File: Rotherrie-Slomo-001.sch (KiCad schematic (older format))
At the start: 17 parts, among them U1 TL074

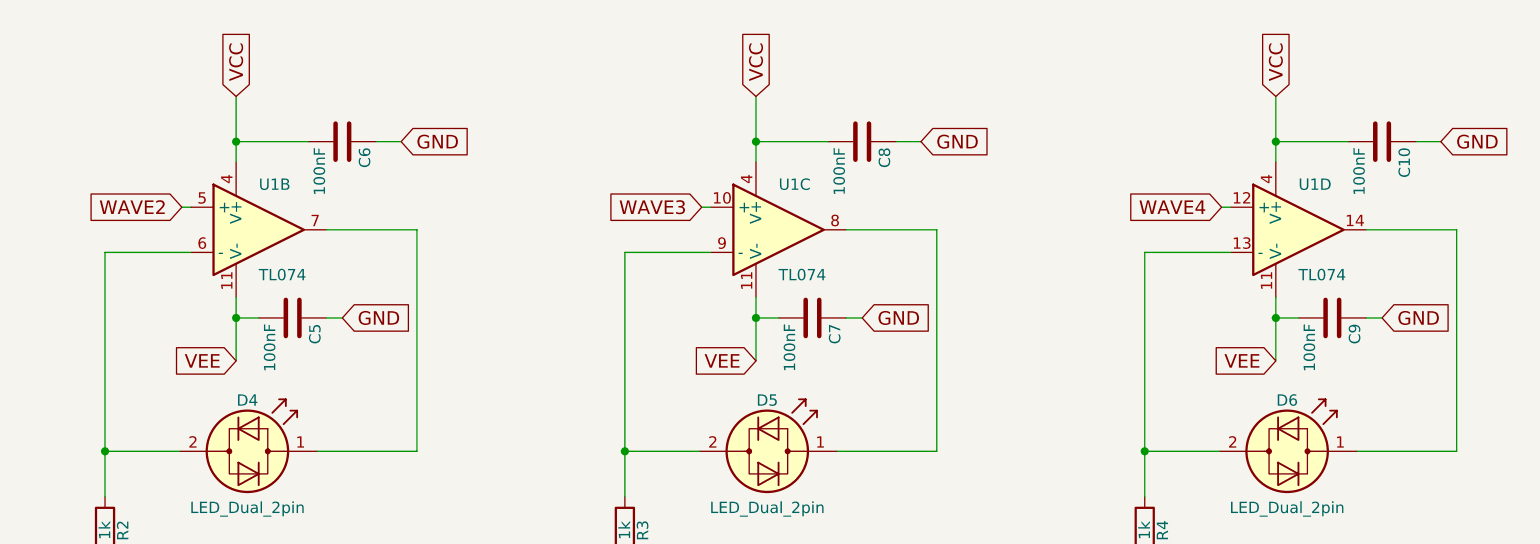
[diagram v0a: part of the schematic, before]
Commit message: Part associations made. 16pin connector reduced to 10 pin
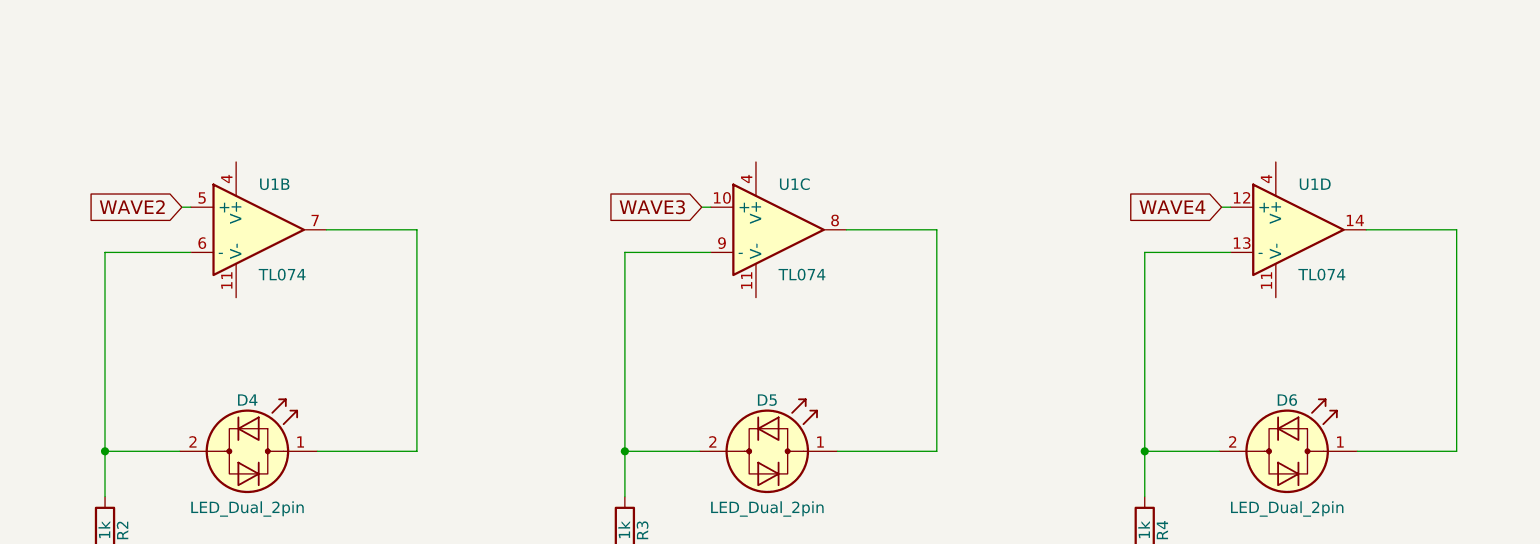
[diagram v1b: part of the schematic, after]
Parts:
- removed C10, C5, C6, C7, C8, C9: 100nF, symbol C
- C3, C4: footprint (none) -> Capacitors_THT:C_Disc_D4.3mm_W1.9mm_P5.00mm
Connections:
- net VCC: no longer U1.4 (V+), U1.4 (V+), U1.4 (V+)
- net VEE: no longer U1.11 (V-), U1.11 (V-), U1.11 (V-)
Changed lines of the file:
@@
 F 0 "C3" H 2625 3140 50  0000 L CNN
 F 1 "100nF" H 2625 2940 50  0000 L CNN
-F 2 "" H 2638 2890 50  0001 C CNN
+F 2 "Capacitors_THT:C_Disc_D4.3mm_W1.9mm_P5.00mm" H 2638 2890 50  0001 C CNN
 F 3 "" H 2600 3040 50  0001 C CNN
 	1    2600 3040
@@
 F 0 "C4" H 2845 2360 50  0000 L CNN
 F 1 "100nF" H 2845 2160 50  0000 L CNN
-F 2 "" H 2858 2110 50  0001 C CNN
+F 2 "Capacitors_THT:C_Disc_D4.3mm_W1.9mm_P5.00mm" H 2858 2110 50  0001 C CNN
 F 3 "" H 2820 2260 50  0001 C CNN
 	1    2820 2260
@@
 	1    0    0    -1
 $EndComp
-Text GLabel 4650 2060 1    60   Input ~ 0
-VCC
-Text GLabel 4650 3230 0    60   Input ~ 0
-VEE
 $Comp
 L LED_Dual_2pin D4
@@
 	1    0    0    -1
 $EndComp
-$Comp
-L C C5
-U 1 1 59B166A0
-P 4900 3040
-F 0 "C5" H 4925 3140 50  0000 L CNN
-F 1 "100nF" H 4925 2940 50  0000 L CNN
-F 2 "" H 4938 2890 50  0001 C CNN
-F 3 "" H 4900 3040 50  0001 C CNN
-	1    4900 3040
-	0    1    1    0
-$EndComp
-Text GLabel 5120 3040 2    60   Input ~ 0
-GND
-$Comp
-L C C6
-U 1 1 59B166B5
-P 5120 2260
-F 0 "C6" H 5145 2360 50  0000 L CNN
-F 1 "100nF" H 5145 2160 50  0000 L CNN
-F 2 "" H 5158 2110 50  0001 C CNN
-F 3 "" H 5120 2260 50  0001 C CNN
-	1    5120 2260
-	0    1    1    0
-$EndComp
-Text GLabel 5380 2260 2    60   Input ~ 0
-GND
 Text GLabel 6370 4300 3    60   Input ~ 0
 GND
@@
 	1    0    0    -1
 $EndComp
-Text GLabel 6950 2060 1    60   Input ~ 0
-VCC
-Text GLabel 6950 3230 0    60   Input ~ 0
-VEE
 $Comp
 L LED_Dual_2pin D5
@@
 	1    0    0    -1
 $EndComp
-$Comp
-L C C7
-U 1 1 59B1681D
-P 7200 3040
-F 0 "C7" H 7225 3140 50  0000 L CNN
-F 1 "100nF" H 7225 2940 50  0000 L CNN
-F 2 "" H 7238 2890 50  0001 C CNN
-F 3 "" H 7200 3040 50  0001 C CNN
-	1    7200 3040
-	0    1    1    0
-$EndComp
-Text GLabel 7420 3040 2    60   Input ~ 0
-GND
-$Comp
-L C C8
-U 1 1 59B16832
-P 7420 2260
-F 0 "C8" H 7445 2360 50  0000 L CNN
-F 1 "100nF" H 7445 2160 50  0000 L CNN
-F 2 "" H 7458 2110 50  0001 C CNN
-F 3 "" H 7420 2260 50  0001 C CNN
-	1    7420 2260
-	0    1    1    0
-$EndComp
-Text GLabel 7680 2260 2    60   Input ~ 0
-GND
 Text GLabel 8670 4300 3    60   Input ~ 0
 GND
@@
 	1    0    0    -1
 $EndComp
-Text GLabel 9250 2060 1    60   Input ~ 0
-VCC
-Text GLabel 9250 3230 0    60   Input ~ 0
-VEE
 $Comp
 L LED_Dual_2pin D6
@@
 	1    0    0    -1
 $EndComp
-$Comp
-L C C9
-U 1 1 59B16A0F
-P 9500 3040
-F 0 "C9" H 9525 3140 50  0000 L CNN
-F 1 "100nF" H 9525 2940 50  0000 L CNN
-F 2 "" H 9538 2890 50  0001 C CNN
-F 3 "" H 9500 3040 50  0001 C CNN
-	1    9500 3040
-	0    1    1    0
-$EndComp
-Text GLabel 9720 3040 2    60   Input ~ 0
-GND
-$Comp
-L C C10
-U 1 1 59B16A24
-P 9720 2260
-F 0 "C10" H 9745 2360 50  0000 L CNN
-F 1 "100nF" H 9745 2160 50  0000 L CNN
-F 2 "" H 9758 2110 50  0001 C CNN
-F 3 "" H 9720 2260 50  0001 C CNN
-	1    9720 2260
-	0    1    1    0
-$EndComp
-Text GLabel 9980 2260 2    60   Input ~ 0
-GND
 Wire Wire Line
 	2350 2060 2350 2350
@@
 	2970 2260 3080 2260
 Wire Wire Line
-	4650 2060 4650 2350
-Wire Wire Line
 	5050 2650 5450 2650
 Wire Wire Line
@@
 	4070 4300 4070 4130
 Wire Wire Line
-	4750 3040 4650 3040
-Connection ~ 4650 3040
-Wire Wire Line
 	5450 2650 5450 3630
-Wire Wire Line
-	5120 3040 5050 3040
 Wire Wire Line
 	5450 3630 5010 3630
@@
 Connection ~ 4070 3630
 Wire Wire Line
-	4650 2950 4650 3230
-Wire Wire Line
 	4410 2550 4450 2550
 Wire Wire Line
-	4970 2260 4650 2260
-Connection ~ 4650 2260
-Wire Wire Line
-	5270 2260 5380 2260
-Wire Wire Line
-	6950 2060 6950 2350
-Wire Wire Line
 	7350 2650 7750 2650
 Wire Wire Line
@@
 	6370 4300 6370 4130
 Wire Wire Line
-	7050 3040 6950 3040
-Connection ~ 6950 3040
-Wire Wire Line
 	7750 2650 7750 3630
-Wire Wire Line
-	7420 3040 7350 3040
 Wire Wire Line
 	7750 3630 7310 3630
@@
 Connection ~ 6370 3630
 Wire Wire Line
-	6950 2950 6950 3230
-Wire Wire Line
 	6710 2550 6750 2550
 Wire Wire Line
-	7270 2260 6950 2260
-Connection ~ 6950 2260
-Wire Wire Line
-	7570 2260 7680 2260
-Wire Wire Line
-	9250 2060 9250 2350
-Wire Wire Line
 	9650 2650 10050 2650
 Wire Wire Line
@@
 	8670 4300 8670 4130
 Wire Wire Line
-	9350 3040 9250 3040
-Connection ~ 9250 3040
-Wire Wire Line
 	10050 2650 10050 3630
-Wire Wire Line
-	9720 3040 9650 3040
 Wire Wire Line
 	10050 3630 9610 3630
@@
 Connection ~ 8670 3630
 Wire Wire Line
-	9250 2950 9250 3230
-Wire Wire Line
 	9010 2550 9050 2550
-Wire Wire Line
-	9570 2260 9250 2260
-Connection ~ 9250 2260
-Wire Wire Line
-	9870 2260 9980 2260
 $EndSCHEMATC

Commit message: Added jack connectors to schematic
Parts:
- D3, D4, D5, D6: footprint (none) -> LEDs:LED_D3.0mm
- R1, R2, R3, R4: footprint (none) -> Resistors_THT:R_Axial_DIN0207_L6.3mm_D2.5mm_P7.62mm_Horizontal
- U1: footprint (none) -> Housings_DIP:DIP-14_W7.62mm_Socket
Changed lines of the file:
@@
 F 0 "U1" H 2450 2850 50  0000 L CNN
 F 1 "TL074" H 2450 2450 50  0000 L CNN
-F 2 "" H 2400 2750 50  0001 C CNN
+F 2 "Housings_DIP:DIP-14_W7.62mm_Socket" H 2400 2750 50  0001 C CNN
 F 3 "" H 2500 2850 50  0001 C CNN
 	1    2450 2650
@@
 F 0 "D3" H 2400 3855 50  0000 C CNN
 F 1 "LED_Dual_2pin" H 2400 3380 50  0000 C CNN
-F 2 "" H 2400 3630 50  0001 C CNN
+F 2 "LEDs:LED_D3.0mm" H 2400 3630 50  0001 C CNN
 F 3 "" H 2400 3630 50  0001 C CNN
 	1    2400 3630
@@
 F 0 "R1" V 1850 3980 50  0000 C CNN
 F 1 "1k" V 1770 3980 50  0000 C CNN
-F 2 "" V 1700 3980 50  0001 C CNN
+F 2 "Resistors_THT:R_Axial_DIN0207_L6.3mm_D2.5mm_P7.62mm_Horizontal" V 1700 3980 50  0001 C CNN
 F 3 "" H 1770 3980 50  0001 C CNN
 	1    1770 3980
@@
 F 0 "U1" H 4750 2850 50  0000 L CNN
 F 1 "TL074" H 4750 2450 50  0000 L CNN
-F 2 "" H 4700 2750 50  0001 C CNN
+F 2 "Housings_DIP:DIP-14_W7.62mm_Socket" H 4700 2750 50  0001 C CNN
 F 3 "" H 4800 2850 50  0001 C CNN
 	2    4750 2650
@@
 F 0 "D4" H 4700 3855 50  0000 C CNN
 F 1 "LED_Dual_2pin" H 4700 3380 50  0000 C CNN
-F 2 "" H 4700 3630 50  0001 C CNN
+F 2 "LEDs:LED_D3.0mm" H 4700 3630 50  0001 C CNN
 F 3 "" H 4700 3630 50  0001 C CNN
 	1    4700 3630
@@
 F 0 "R2" V 4150 3980 50  0000 C CNN
 F 1 "1k" V 4070 3980 50  0000 C CNN
-F 2 "" V 4000 3980 50  0001 C CNN
+F 2 "Resistors_THT:R_Axial_DIN0207_L6.3mm_D2.5mm_P7.62mm_Horizontal" V 4000 3980 50  0001 C CNN
 F 3 "" H 4070 3980 50  0001 C CNN
 	1    4070 3980
@@
 F 0 "U1" H 7050 2850 50  0000 L CNN
 F 1 "TL074" H 7050 2450 50  0000 L CNN
-F 2 "" H 7000 2750 50  0001 C CNN
+F 2 "Housings_DIP:DIP-14_W7.62mm_Socket" H 7000 2750 50  0001 C CNN
 F 3 "" H 7100 2850 50  0001 C CNN
 	3    7050 2650
@@
 F 0 "D5" H 7000 3855 50  0000 C CNN
 F 1 "LED_Dual_2pin" H 7000 3380 50  0000 C CNN
-F 2 "" H 7000 3630 50  0001 C CNN
+F 2 "LEDs:LED_D3.0mm" H 7000 3630 50  0001 C CNN
 F 3 "" H 7000 3630 50  0001 C CNN
 	1    7000 3630
@@
 F 0 "R3" V 6450 3980 50  0000 C CNN
 F 1 "1k" V 6370 3980 50  0000 C CNN
-F 2 "" V 6300 3980 50  0001 C CNN
+F 2 "Resistors_THT:R_Axial_DIN0207_L6.3mm_D2.5mm_P7.62mm_Horizontal" V 6300 3980 50  0001 C CNN
 F 3 "" H 6370 3980 50  0001 C CNN
 	1    6370 3980
@@
 F 0 "U1" H 9350 2850 50  0000 L CNN
 F 1 "TL074" H 9350 2450 50  0000 L CNN
-F 2 "" H 9300 2750 50  0001 C CNN
+F 2 "Housings_DIP:DIP-14_W7.62mm_Socket" H 9300 2750 50  0001 C CNN
 F 3 "" H 9400 2850 50  0001 C CNN
 	4    9350 2650
@@
 F 0 "D6" H 9300 3855 50  0000 C CNN
 F 1 "LED_Dual_2pin" H 9300 3380 50  0000 C CNN
-F 2 "" H 9300 3630 50  0001 C CNN
+F 2 "LEDs:LED_D3.0mm" H 9300 3630 50  0001 C CNN
 F 3 "" H 9300 3630 50  0001 C CNN
 	1    9300 3630
@@
 F 0 "R4" V 8750 3980 50  0000 C CNN
 F 1 "1k" V 8670 3980 50  0000 C CNN
-F 2 "" V 8600 3980 50  0001 C CNN
+F 2 "Resistors_THT:R_Axial_DIN0207_L6.3mm_D2.5mm_P7.62mm_Horizontal" V 8600 3980 50  0001 C CNN
 F 3 "" H 8670 3980 50  0001 C CNN
 	1    8670 3980

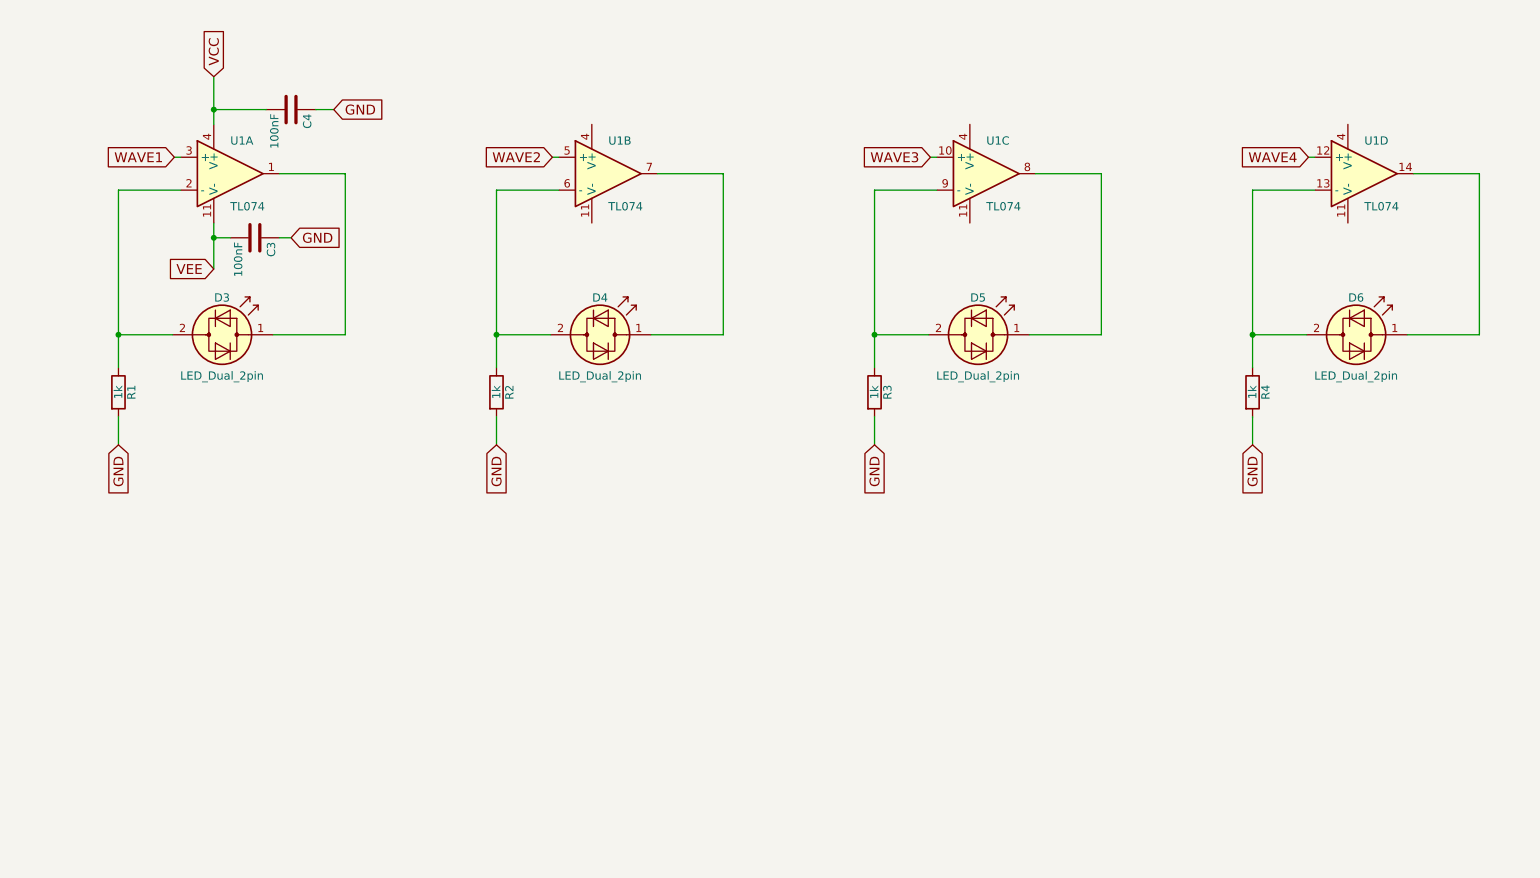
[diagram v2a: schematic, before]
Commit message: Rerouting from logic to controller board
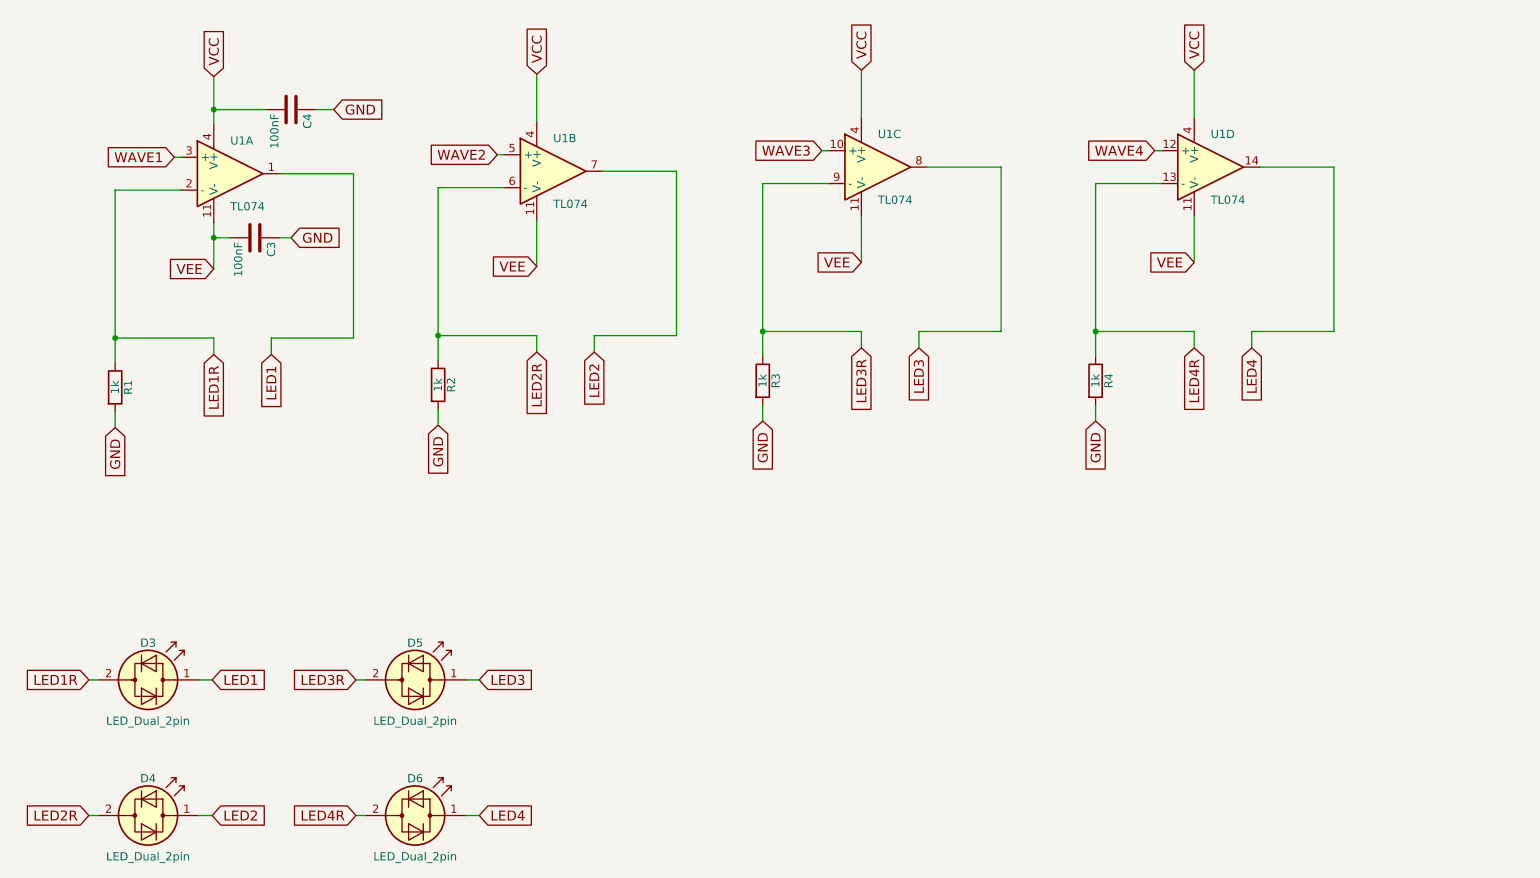
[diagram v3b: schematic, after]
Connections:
- net VCC: now also U1.4 (V+), U1.4 (V+), U1.4 (V+)
- net VEE: now also U1.11 (V-), U1.11 (V-), U1.11 (V-)
- net LED1: now reaches D3.1 (KA), U1.1
- net LED1R: now reaches D3.2 (AK), R1.1, U1.2 (-)
- net LED2R: now reaches D4.2 (AK), R2.1, U1.6 (-)
- net LED2: now reaches D4.1 (KA), U1.7
- net LED3: now reaches D5.1 (KA), U1.8
- net LED3R: now reaches D5.2 (AK), R3.1, U1.9 (-)
- net LED4R: now reaches D6.2 (AK), R4.1, U1.13 (-)
- net LED4: now reaches D6.1 (KA), U1.14
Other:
- moved on the sheet: D3, R1
